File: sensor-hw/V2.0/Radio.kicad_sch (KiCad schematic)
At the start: 57 parts, among them J7 Conn_Coaxial, X204 32Mhz, X503 32Mhz

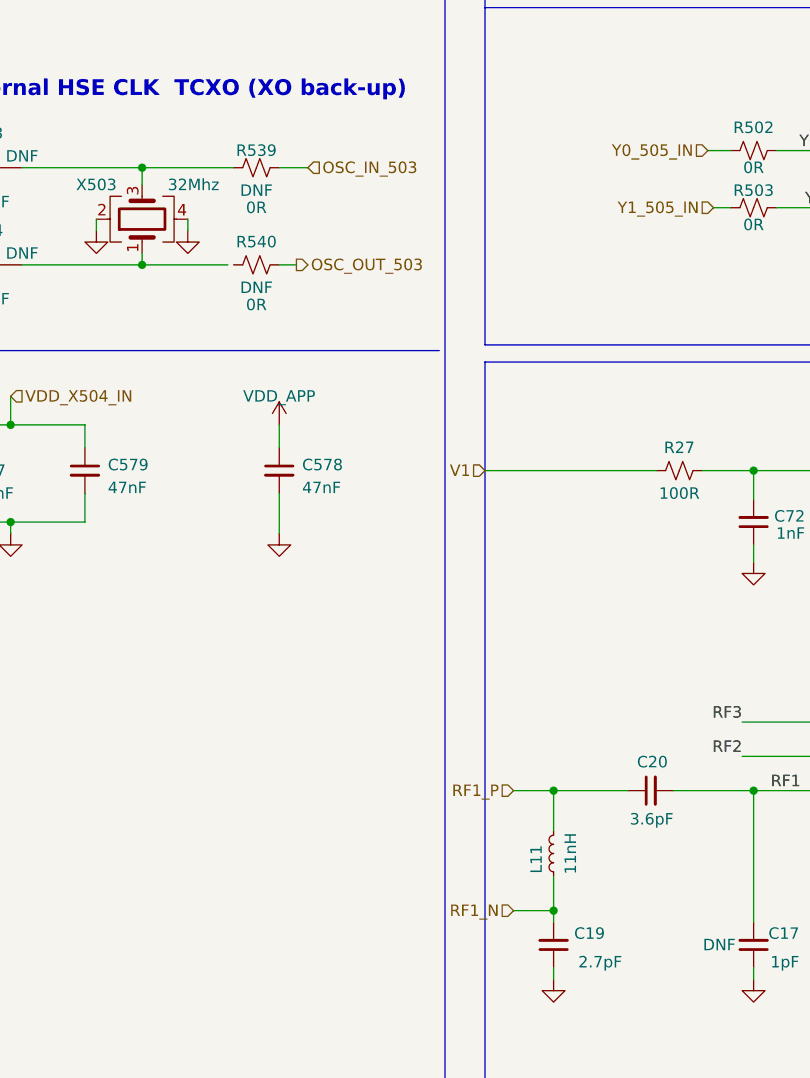
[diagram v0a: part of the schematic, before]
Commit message: rearranged heirchal block wiring for better representation.
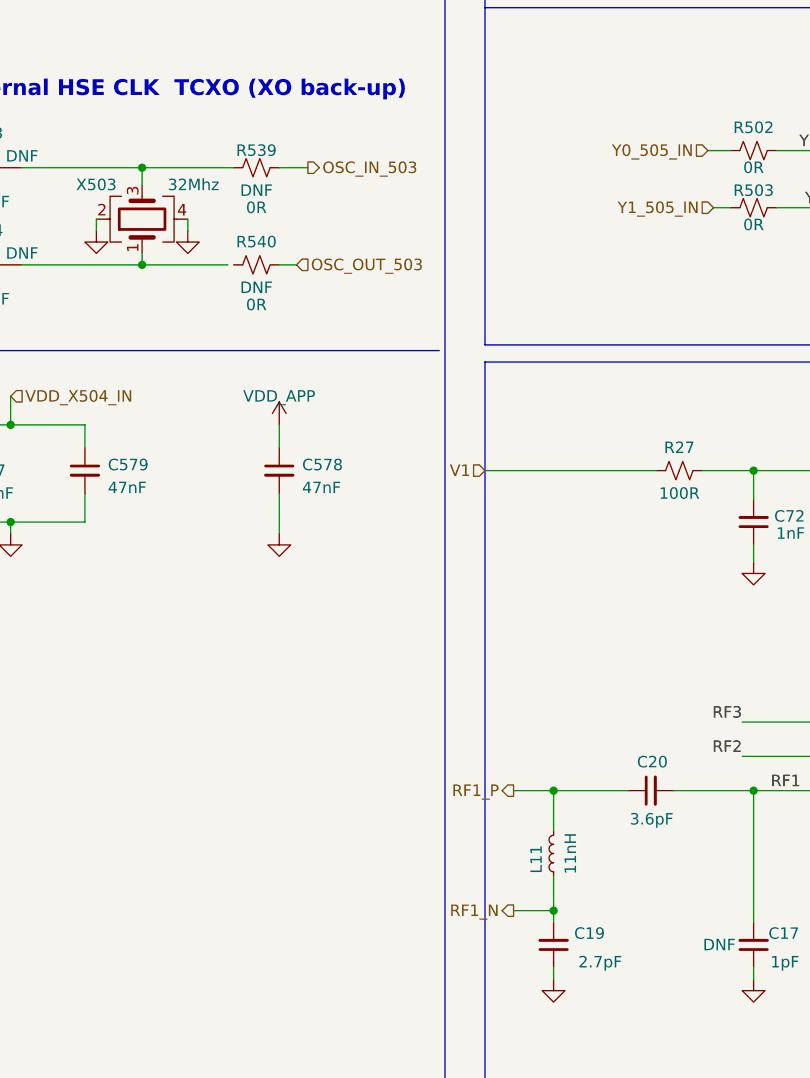
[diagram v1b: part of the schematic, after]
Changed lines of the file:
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@@
     (effects (font (size 1.27 1.27)) (justify left bottom))
   )
-  (hierarchical_label "OSC_OUT_503" (shape output) (at 55.245 95.885 0) (fields_autoplaced)
+  (hierarchical_label "OSC_OUT_503" (shape input) (at 55.245 95.885 0) (fields_autoplaced)
     (effects (font (size 1.27 1.27)) (justify left))
   )
@@
     (effects (font (size 1.27 1.27)) (justify right))
   )
-  (hierarchical_label "OSC_IN_503" (shape input) (at 56.515 85.09 0) (fields_autoplaced)
+  (hierarchical_label "OSC_IN_503" (shape output) (at 56.515 85.09 0) (fields_autoplaced)
     (effects (font (size 1.27 1.27)) (justify left))
   )
-  (hierarchical_label "RF1_P" (shape input) (at 79.375 154.305 180) (fields_autoplaced)
+  (hierarchical_label "RF1_P" (shape output) (at 79.375 154.305 180) (fields_autoplaced)
     (effects (font (size 1.27 1.27)) (justify right))
   )
@@
     (effects (font (size 1.27 1.27)) (justify left))
   )
-  (hierarchical_label "RF1_N" (shape input) (at 79.375 167.64 180) (fields_autoplaced)
+  (hierarchical_label "RF1_N" (shape output) (at 79.375 167.64 180) (fields_autoplaced)
     (effects (font (size 1.27 1.27)) (justify right))
   )
